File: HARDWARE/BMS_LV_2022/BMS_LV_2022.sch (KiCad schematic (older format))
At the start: 8 parts

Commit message: Hardware Update 2
First verison of the scheme finished
+Power section
+eFuse section
+Current Sensor section
+Connectors section
+Debug LEDs
+STM32L4P5RET6 all signals configuration
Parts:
- added C?: 100n, symbol Device:C_Small
- added C? (x2): 22p, symbol Device:C_Small
- added D? (x4): LED, symbol Device:LED
- added J?: Conn_01x12_Male, symbol Connector:Conn_01x12_Male
- added J?: Conn_01x06_Male, symbol Connector:Conn_01x06_Male
- added J?: USB_B_Mini, symbol Connector:USB_B_Mini
- added R? (x2): 100k, symbol Device:R_Small
- added R? (x2): 30, symbol Device:R_Small
- added R? (x4): R_Small, symbol Device:R_Small
- added SW?: SW_Push, symbol Switch:SW_Push
- added Y?: Crystal, symbol Device:Crystal
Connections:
- net labels added: +5VD, CAN-RX, CAN-TX, CANH, CANL, CS_IP+, CurrentSensor_Out, Interlock, LED_1, LED_2, LED_3, LED_4, NRST, SW-CLK, SW-DIO, SW-GND, SW-NRST, SW-VDD, Switch_Signal, USB-DM, USB-DP, VCC, V_Out
- wire segments 56 -> 163
- no-connect marks 0 -> 1
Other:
- note added: "Connectors"
- note added: "Debug LEDs"
- note added: "Reset Button"
- note added: "Shorted when \nconnector is connected"
- note added: "USB conn on box cover? / autosport?"
- moved on the sheet: C?, L?

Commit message: Hardware update; -changes after team review;
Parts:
- C? (x7): value 100n -> 100nF
- C? (x2): value 22p -> 22pF
- R? (x4): value R_Small -> 470
- U?: symbol STM32L4P5RET6:STM32L4P5RET6 -> BMS_LV_2022-rescue:STM32L4P5RET6-STM32L4P5RET6
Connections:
- net labels added: VCC_Pin
- wire segments 163 -> 167
- no-connect marks 1 -> 31
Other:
- note added: "?"
- note added: "Autosport"
- note added: "PIN #16"
- note added: "PIN #20"
- note added: "SWD"
- note added: "USB"
- note removed: "USB conn on box cover? / autosport?"
- moved on the sheet: C?, J?

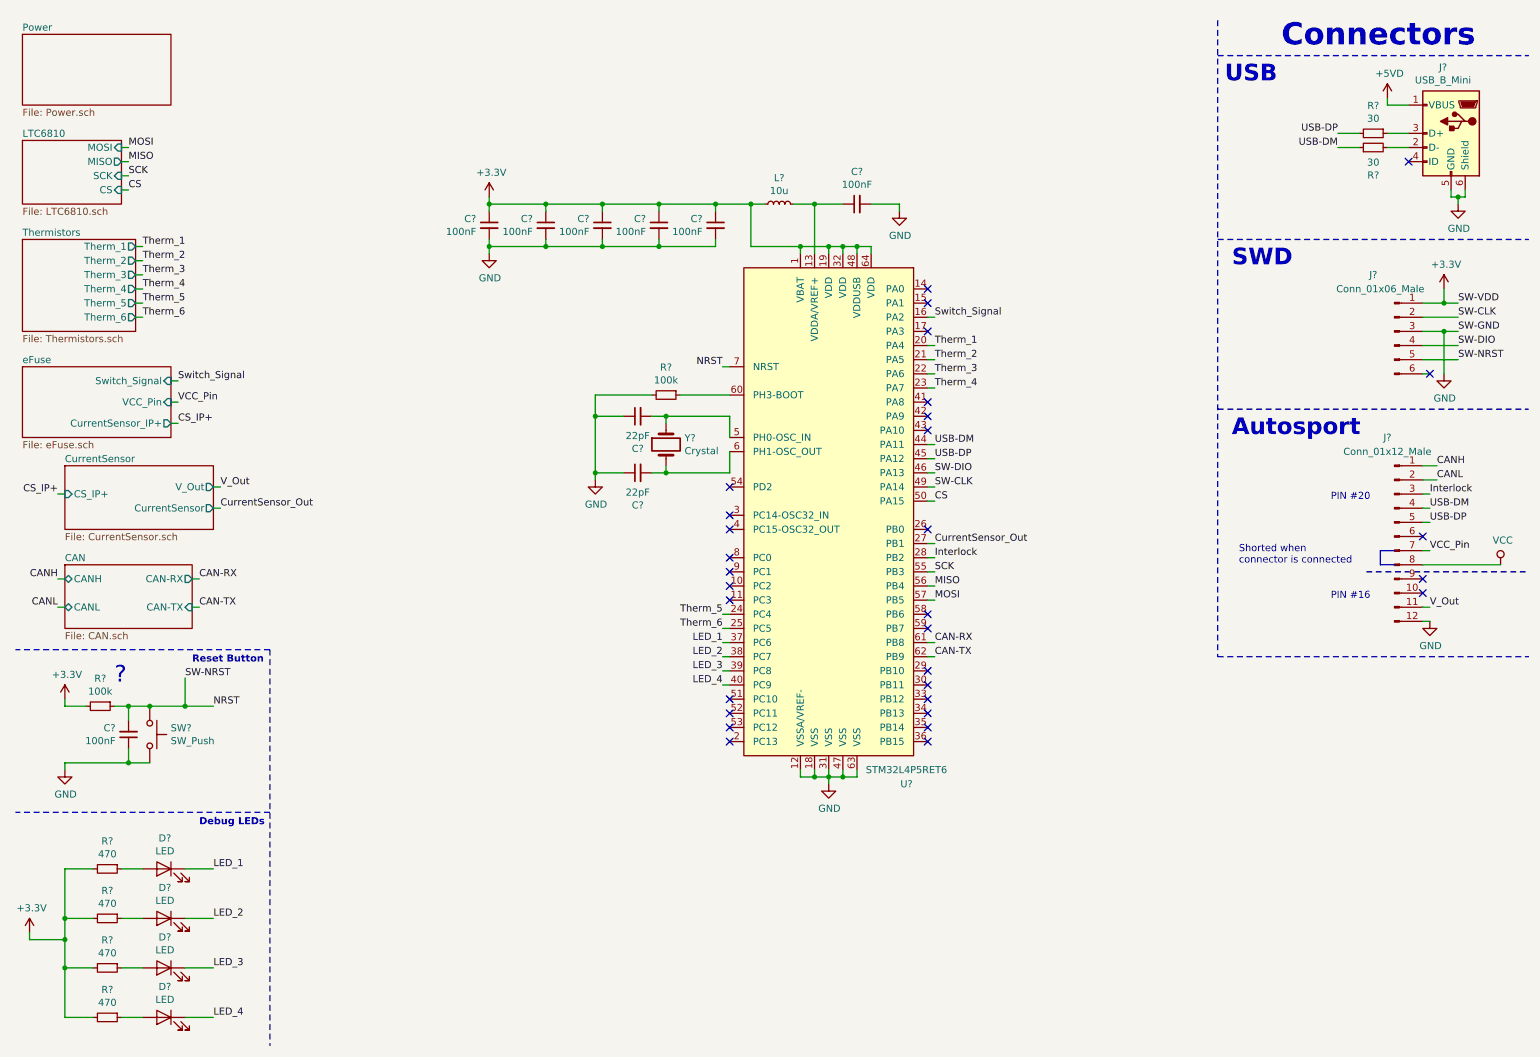
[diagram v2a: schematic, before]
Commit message: Electrical Rules Checker fixes
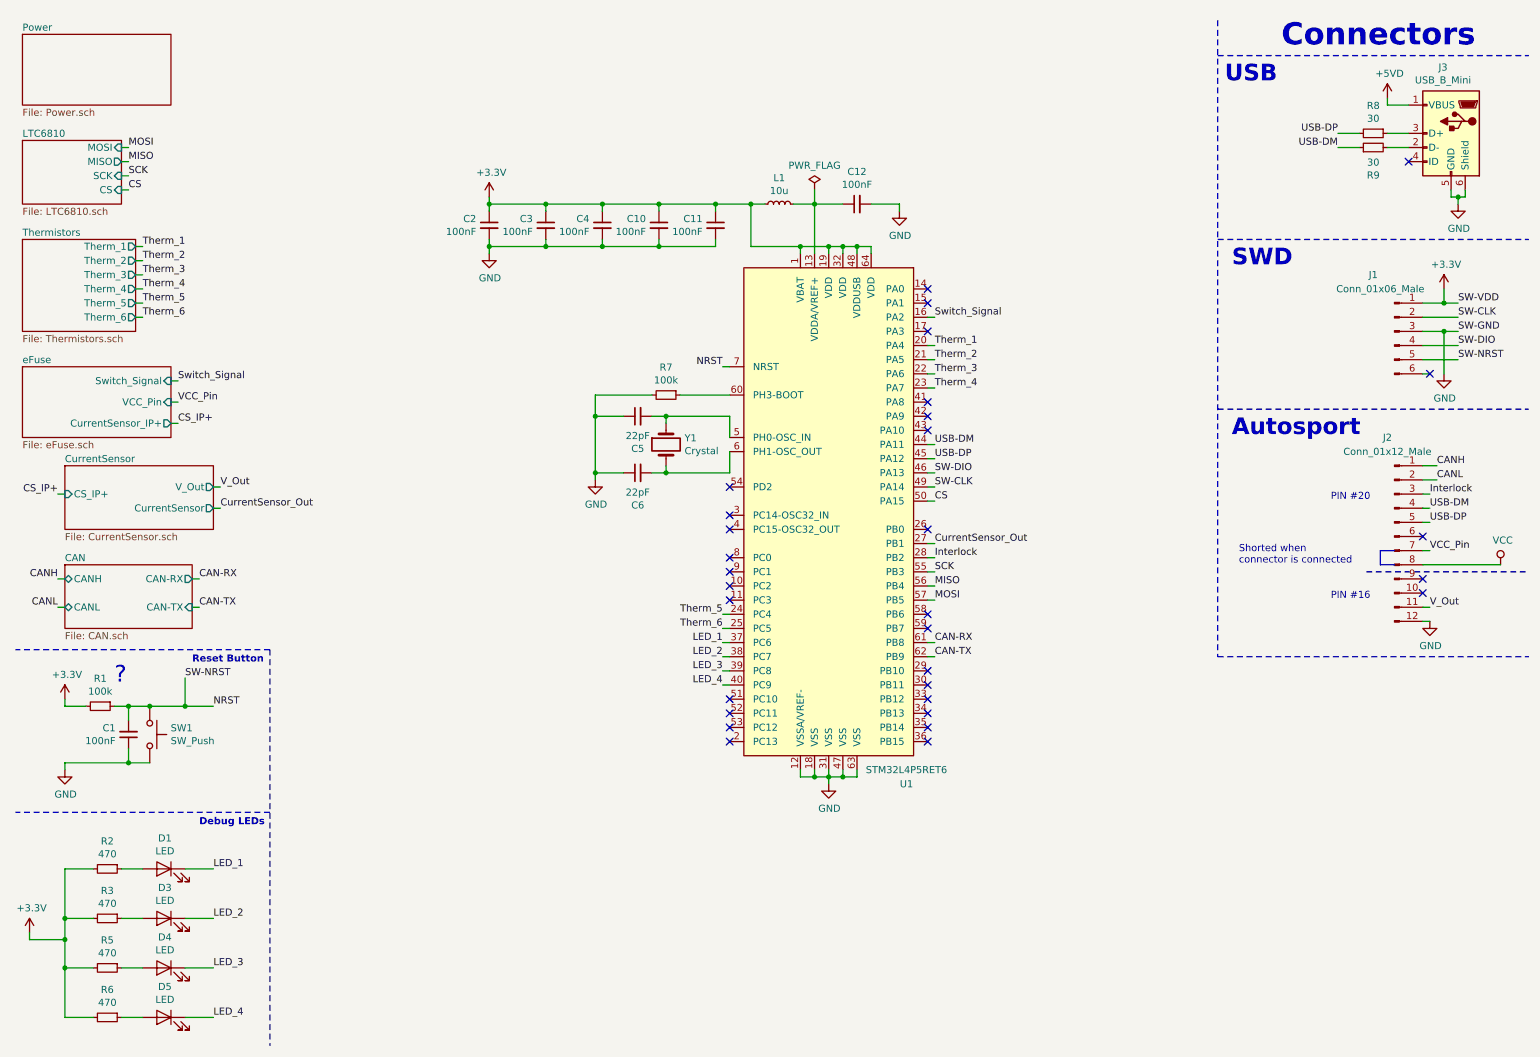
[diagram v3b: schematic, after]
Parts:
- gave numbers to parts that had none: 28

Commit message: Most of the footprints added
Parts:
- C1, C10, C11, C12, C2, C3, C4, C5, C6: footprint (none) -> Capacitor_SMD:C_0603_1608Metric
- D1, D3, D4, D5: footprint (none) -> LED_SMD:LED_0603_1608Metric
- J1: footprint (none) -> Connector_PinHeader_2.54mm:PinHeader_1x06_P2.54mm_Vertical
- J3: footprint (none) -> Connector_USB:USB_Mini-B_AdamTech_MUSB-B5-S-VT-TSMT-1_SMD_Vertical
- L1: footprint (none) -> Inductor_SMD:L_0603_1608Metric
- R1, R2, R3, R5, R6, R7, R8, R9: footprint (none) -> Resistor_SMD:R_0603_1608Metric
- SW1: footprint (none) -> Button_Switch_THT:SW_PUSH_6mm
- Y1: footprint (none) -> Crystal:Crystal_SMD_3225-4Pin_3.2x2.5mm
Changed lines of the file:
@@
 F 0 "C12" V 6221 1800 50  0000 C CNN
 F 1 "100nF" V 6312 1800 50  0000 C CNN
-F 2 "" H 6450 1800 50  0001 C CNN
+F 2 "Capacitor_SMD:C_0603_1608Metric" H 6450 1800 50  0001 C CNN
 F 3 "~" H 6450 1800 50  0001 C CNN
 	1    6450 1800
@@
 F 0 "L1" V 6085 1800 50  0000 C CNN
 F 1 "10u" V 5994 1800 50  0000 C CNN
-F 2 "" H 5900 1800 50  0001 C CNN
+F 2 "Inductor_SMD:L_0603_1608Metric" H 5900 1800 50  0001 C CNN
 F 3 "~" H 5900 1800 50  0001 C CNN
 	1    5900 1800
@@
 F 0 "C2" H 3942 1996 50  0000 L CNN
 F 1 "100nF" H 3942 1905 50  0000 L CNN
-F 2 "" H 3850 1950 50  0001 C CNN
+F 2 "Capacitor_SMD:C_0603_1608Metric" H 3850 1950 50  0001 C CNN
 F 3 "~" H 3850 1950 50  0001 C CNN
 	1    3850 1950
@@
 F 0 "C3" H 4342 1996 50  0000 L CNN
 F 1 "100nF" H 4342 1905 50  0000 L CNN
-F 2 "" H 4250 1950 50  0001 C CNN
+F 2 "Capacitor_SMD:C_0603_1608Metric" H 4250 1950 50  0001 C CNN
 F 3 "~" H 4250 1950 50  0001 C CNN
 	1    4250 1950
@@
 F 0 "C11" H 5542 1996 50  0000 L CNN
 F 1 "100nF" H 5542 1905 50  0000 L CNN
-F 2 "" H 5450 1950 50  0001 C CNN
+F 2 "Capacitor_SMD:C_0603_1608Metric" H 5450 1950 50  0001 C CNN
 F 3 "~" H 5450 1950 50  0001 C CNN
 	1    5450 1950
@@
 F 0 "C10" H 5142 1996 50  0000 L CNN
 F 1 "100nF" H 5142 1905 50  0000 L CNN
-F 2 "" H 5050 1950 50  0001 C CNN
+F 2 "Capacitor_SMD:C_0603_1608Metric" H 5050 1950 50  0001 C CNN
 F 3 "~" H 5050 1950 50  0001 C CNN
 	1    5050 1950
@@
 F 0 "C4" H 4742 1996 50  0000 L CNN
 F 1 "100nF" H 4742 1905 50  0000 L CNN
-F 2 "" H 4650 1950 50  0001 C CNN
+F 2 "Capacitor_SMD:C_0603_1608Metric" H 4650 1950 50  0001 C CNN
 F 3 "~" H 4650 1950 50  0001 C CNN
 	1    4650 1950
@@
 F 0 "J1" H 10100 3100 50  0000 C CNN
 F 1 "Conn_01x06_Male" H 10150 3000 50  0000 C CNN
-F 2 "" H 10250 2700 50  0001 C CNN
+F 2 "Connector_PinHeader_2.54mm:PinHeader_1x06_P2.54mm_Vertical" H 10250 2700 50  0001 C CNN
 F 3 "~" H 10250 2700 50  0001 C CNN
 	1    10250 2700
@@
 F 0 "SW1" V 1404 5698 50  0000 L CNN
 F 1 "SW_Push" V 1495 5698 50  0000 L CNN
-F 2 "" H 1450 5750 50  0001 C CNN
+F 2 "Button_Switch_THT:SW_PUSH_6mm" H 1450 5750 50  0001 C CNN
 F 3 "~" H 1450 5750 50  0001 C CNN
 	1    1450 5550
@@
 F 0 "C1" H 1208 5504 50  0000 R CNN
 F 1 "100nF" H 1208 5595 50  0000 R CNN
-F 2 "" H 1300 5550 50  0001 C CNN
+F 2 "Capacitor_SMD:C_0603_1608Metric" H 1300 5550 50  0001 C CNN
 F 3 "~" H 1300 5550 50  0001 C CNN
 	1    1300 5550
@@
 F 0 "R1" V 904 5350 50  0000 C CNN
 F 1 "100k" V 995 5350 50  0000 C CNN
-F 2 "" H 1100 5350 50  0001 C CNN
+F 2 "Resistor_SMD:R_0603_1608Metric" H 1100 5350 50  0001 C CNN
 F 3 "~" H 1100 5350 50  0001 C CNN
 	1    1100 5350
@@
 F 0 "Y1" V 5054 3369 50  0000 R CNN
 F 1 "Crystal" V 5145 3369 50  0000 R CNN
-F 2 "" H 5100 3500 50  0001 C CNN
+F 2 "Crystal:Crystal_SMD_3225-4Pin_3.2x2.5mm" H 5100 3500 50  0001 C CNN
 F 3 "~" H 5100 3500 50  0001 C CNN
 	1    5100 3500
@@
 F 0 "C6" V 5129 3700 50  0000 C CNN
 F 1 "22pF" V 5038 3700 50  0000 C CNN
-F 2 "" H 4900 3700 50  0001 C CNN
+F 2 "Capacitor_SMD:C_0603_1608Metric" H 4900 3700 50  0001 C CNN
 F 3 "~" H 4900 3700 50  0001 C CNN
 	1    4900 3700
@@
 F 0 "R7" V 4904 3150 50  0000 C CNN
 F 1 "100k" V 4995 3150 50  0000 C CNN
-F 2 "" H 5100 3150 50  0001 C CNN
+F 2 "Resistor_SMD:R_0603_1608Metric" H 5100 3150 50  0001 C CNN
 F 3 "~" H 5100 3150 50  0001 C CNN
 	1    5100 3150
@@
 F 0 "J3" H 10707 1767 50  0000 C CNN
 F 1 "USB_B_Mini" H 10707 1676 50  0000 C CNN
-F 2 "" H 10800 1250 50  0001 C CNN
+F 2 "Connector_USB:USB_Mini-B_AdamTech_MUSB-B5-S-VT-TSMT-1_SMD_Vertical" H 10800 1250 50  0001 C CNN
 F 3 "~" H 10800 1250 50  0001 C CNN
 	1    10650 1300
@@
 F 0 "R8" V 9904 1300 50  0000 C CNN
 F 1 "30" V 9995 1300 50  0000 C CNN
-F 2 "" H 10100 1300 50  0001 C CNN
+F 2 "Resistor_SMD:R_0603_1608Metric" H 10100 1300 50  0001 C CNN
 F 3 "~" H 10100 1300 50  0001 C CNN
 	1    10100 1300
@@
 F 0 "R9" V 9904 1400 50  0000 C CNN
 F 1 "30" V 9995 1400 50  0000 C CNN
-F 2 "" H 10100 1400 50  0001 C CNN
+F 2 "Resistor_SMD:R_0603_1608Metric" H 10100 1400 50  0001 C CNN
 F 3 "~" H 10100 1400 50  0001 C CNN
 	1    10100 1400
@@
 F 0 "C5" V 4671 3300 50  0000 C CNN
 F 1 "22pF" V 4762 3300 50  0000 C CNN
-F 2 "" H 4900 3300 50  0001 C CNN
+F 2 "Capacitor_SMD:C_0603_1608Metric" H 4900 3300 50  0001 C CNN
 F 3 "~" H 4900 3300 50  0001 C CNN
 	1    4900 3300
@@
 F 0 "R2" V 954 6500 50  0000 C CNN
 F 1 "470" V 1045 6500 50  0000 C CNN
-F 2 "" H 1150 6500 50  0001 C CNN
+F 2 "Resistor_SMD:R_0603_1608Metric" H 1150 6500 50  0001 C CNN
 F 3 "~" H 1150 6500 50  0001 C CNN
 	1    1150 6500
@@
 F 0 "D1" H 1543 6717 50  0000 C CNN
 F 1 "LED" H 1543 6626 50  0000 C CNN
-F 2 "" H 1550 6500 50  0001 C CNN
+F 2 "LED_SMD:LED_0603_1608Metric" H 1550 6500 50  0001 C CNN
 F 3 "~" H 1550 6500 50  0001 C CNN
 	1    1550 6500
@@
 F 0 "R3" V 954 6850 50  0000 C CNN
 F 1 "470" V 1045 6850 50  0000 C CNN
-F 2 "" H 1150 6850 50  0001 C CNN
+F 2 "Resistor_SMD:R_0603_1608Metric" H 1150 6850 50  0001 C CNN
 F 3 "~" H 1150 6850 50  0001 C CNN
 	1    1150 6850
@@
 F 0 "D3" H 1543 7067 50  0000 C CNN
 F 1 "LED" H 1543 6976 50  0000 C CNN
-F 2 "" H 1550 6850 50  0001 C CNN
+F 2 "LED_SMD:LED_0603_1608Metric" H 1550 6850 50  0001 C CNN
 F 3 "~" H 1550 6850 50  0001 C CNN
 	1    1550 6850
@@
 F 0 "R5" V 954 7200 50  0000 C CNN
 F 1 "470" V 1045 7200 50  0000 C CNN
-F 2 "" H 1150 7200 50  0001 C CNN
+F 2 "Resistor_SMD:R_0603_1608Metric" H 1150 7200 50  0001 C CNN
 F 3 "~" H 1150 7200 50  0001 C CNN
 	1    1150 7200
@@
 F 0 "D4" H 1543 7417 50  0000 C CNN
 F 1 "LED" H 1543 7326 50  0000 C CNN
-F 2 "" H 1550 7200 50  0001 C CNN
+F 2 "LED_SMD:LED_0603_1608Metric" H 1550 7200 50  0001 C CNN
 F 3 "~" H 1550 7200 50  0001 C CNN
 	1    1550 7200
@@
 F 0 "R6" V 954 7550 50  0000 C CNN
 F 1 "470" V 1045 7550 50  0000 C CNN
-F 2 "" H 1150 7550 50  0001 C CNN
+F 2 "Resistor_SMD:R_0603_1608Metric" H 1150 7550 50  0001 C CNN
 F 3 "~" H 1150 7550 50  0001 C CNN
 	1    1150 7550
@@
 F 0 "D5" H 1543 7767 50  0000 C CNN
 F 1 "LED" H 1543 7676 50  0000 C CNN
-F 2 "" H 1550 7550 50  0001 C CNN
+F 2 "LED_SMD:LED_0603_1608Metric" H 1550 7550 50  0001 C CNN
 F 3 "~" H 1550 7550 50  0001 C CNN
 	1    1550 7550

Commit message: PCB layout init
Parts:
- J2: footprint (none) -> footprints:AS214-97PN
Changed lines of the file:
@@
 F 0 "J2" H 10200 4850 50  0000 C CNN
 F 1 "Conn_01x12_Male" H 10200 4750 50  0000 C CNN
-F 2 "" H 10250 4150 50  0001 C CNN
+F 2 "footprints:AS214-97PN" H 10250 4150 50  0001 C CNN
 F 3 "~" H 10250 4150 50  0001 C CNN
 	1    10250 4150

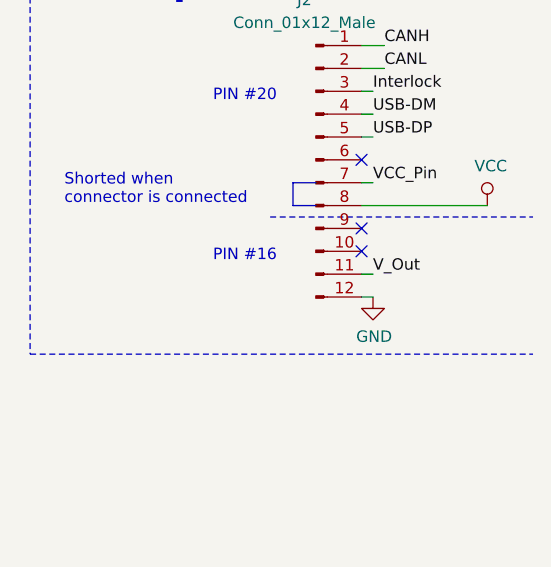
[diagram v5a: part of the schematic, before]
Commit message: PCB update
Parts changed due to smaller footprints
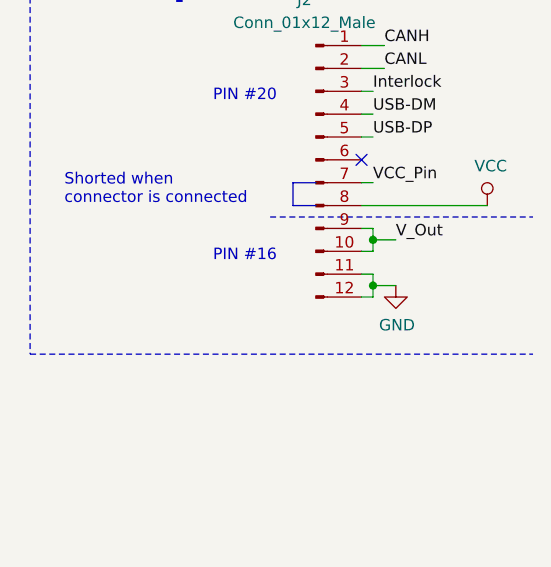
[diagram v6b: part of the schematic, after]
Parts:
- SW1: footprint Button_Switch_THT:SW_PUSH_6mm -> Button_Switch_SMD:SW_SPST_B3U-1000P; Part Number (none) -> B3U-1000PM
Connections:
- net GND: now also J2.11 (Pin_11)
- net V_Out: now also J2.10 (Pin_10), J2.9 (Pin_9); no longer J2.11 (Pin_11)
- no-connect marks 31 -> 29
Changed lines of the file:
@@
 F 0 "SW1" V 1404 5698 50  0000 L CNN
 F 1 "SW_Push" V 1495 5698 50  0000 L CNN
-F 2 "Button_Switch_THT:SW_PUSH_6mm" H 1450 5750 50  0001 C CNN
+F 2 "Button_Switch_SMD:SW_SPST_B3U-1000P" H 1450 5750 50  0001 C CNN
 F 3 "~" H 1450 5750 50  0001 C CNN
+F 4 "B3U-1000PM" H 1450 5550 50  0001 C CNN "Part Number"
 	1    1450 5550
 	0    1    1    0
@@
 Text Label 1650 3350 0    50   ~ 0
 CS_IP+
-Text Label 10500 4650 0    50   ~ 0
+Text Label 10600 4500 0    50   ~ 0
 V_Out
 Wire Wire Line
@@
 L power:GND #PWR010
 U 1 1 62A04D91
-P 10500 4750
-F 0 "#PWR010" H 10500 4500 50  0001 C CNN
-F 1 "GND" H 10505 4577 50  0000 C CNN
-F 2 "" H 10500 4750 50  0001 C CNN
-F 3 "" H 10500 4750 50  0001 C CNN
-	1    10500 4750
-	1    0    0    -1
-$EndComp
-Wire Wire Line
-	10500 4650 10450 4650
+P 10600 4700
+F 0 "#PWR010" H 10600 4450 50  0001 C CNN
+F 1 "GND" H 10605 4527 50  0000 C CNN
+F 2 "" H 10600 4700 50  0001 C CNN
+F 3 "" H 10600 4700 50  0001 C CNN
+	1    10600 4700
+	1    0    0    -1
+$EndComp
+Wire Wire Line
+	10500 4550 10450 4550
 Text Notes 9150 4350 0    50   ~ 0
 Shorted when \nconnector is connected
@@
 NoConn ~ 6950 5500
 NoConn ~ 6950 5600
-NoConn ~ 10450 4550
-NoConn ~ 10450 4450
 NoConn ~ 10450 4150
 NoConn ~ 10350 1500
@@
 	1    0    0    -1
 $EndComp
+Wire Wire Line
+	10500 4450 10450 4450
+Wire Wire Line
+	10500 4450 10500 4500
+Wire Wire Line
+	10500 4500 10600 4500
+Connection ~ 10500 4500
+Wire Wire Line
+	10500 4500 10500 4550
+Wire Wire Line
+	10500 4750 10500 4700
+Wire Wire Line
+	10500 4650 10450 4650
+Wire Wire Line
+	10500 4700 10600 4700
+Connection ~ 10500 4700
+Wire Wire Line
+	10500 4700 10500 4650
 $EndSCHEMATC
